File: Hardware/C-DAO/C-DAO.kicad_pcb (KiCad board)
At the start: 2 copper layers, 50 x 100 mm, 63 parts, among them J1 DIN-5, J2 Bus-connector, J3 AudioJack2, J5 Conn_02x03_Odd_Even, SW1 SW_Push_Dual, SW2 SW_Push_Dual, SW3 SW_Push_Dual, SW4 SW_Push_Dual, U1 ATmega328P-A, U2 L7805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

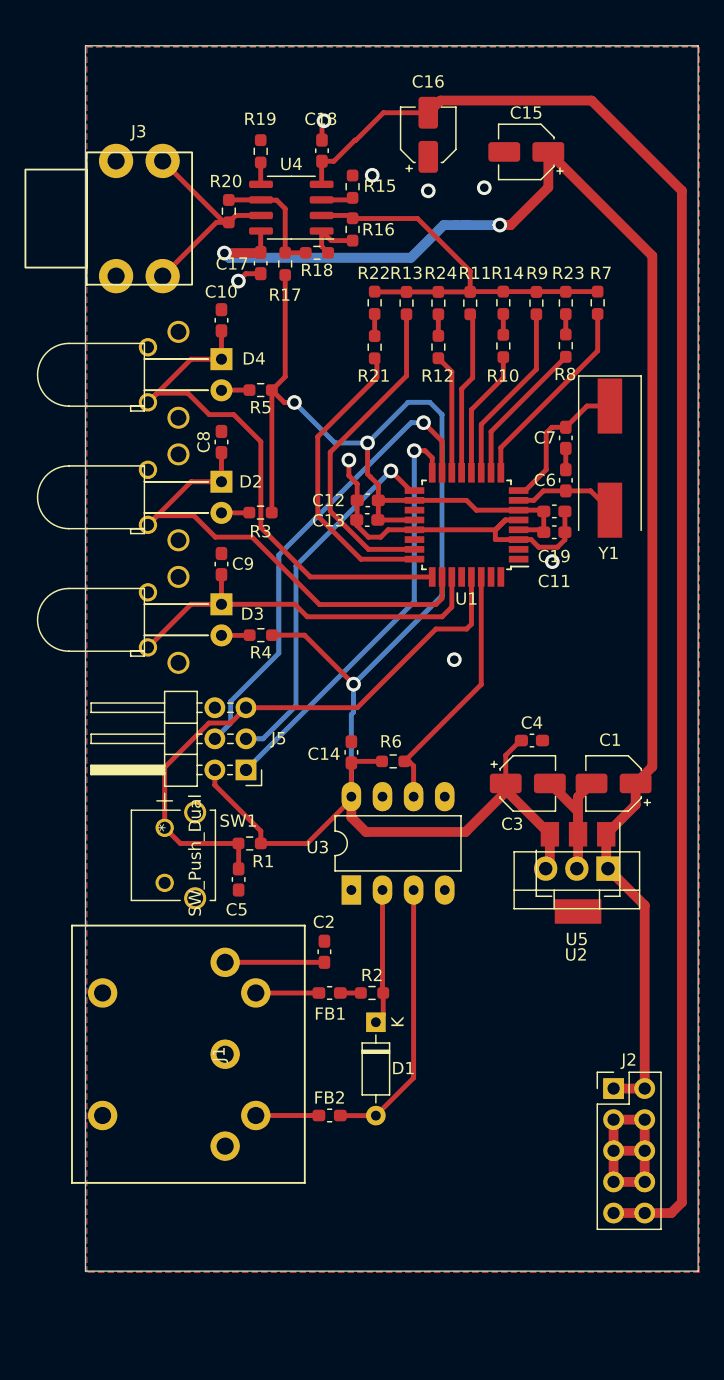
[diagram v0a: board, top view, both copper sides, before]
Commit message: Add production files and latest pcb files with bom
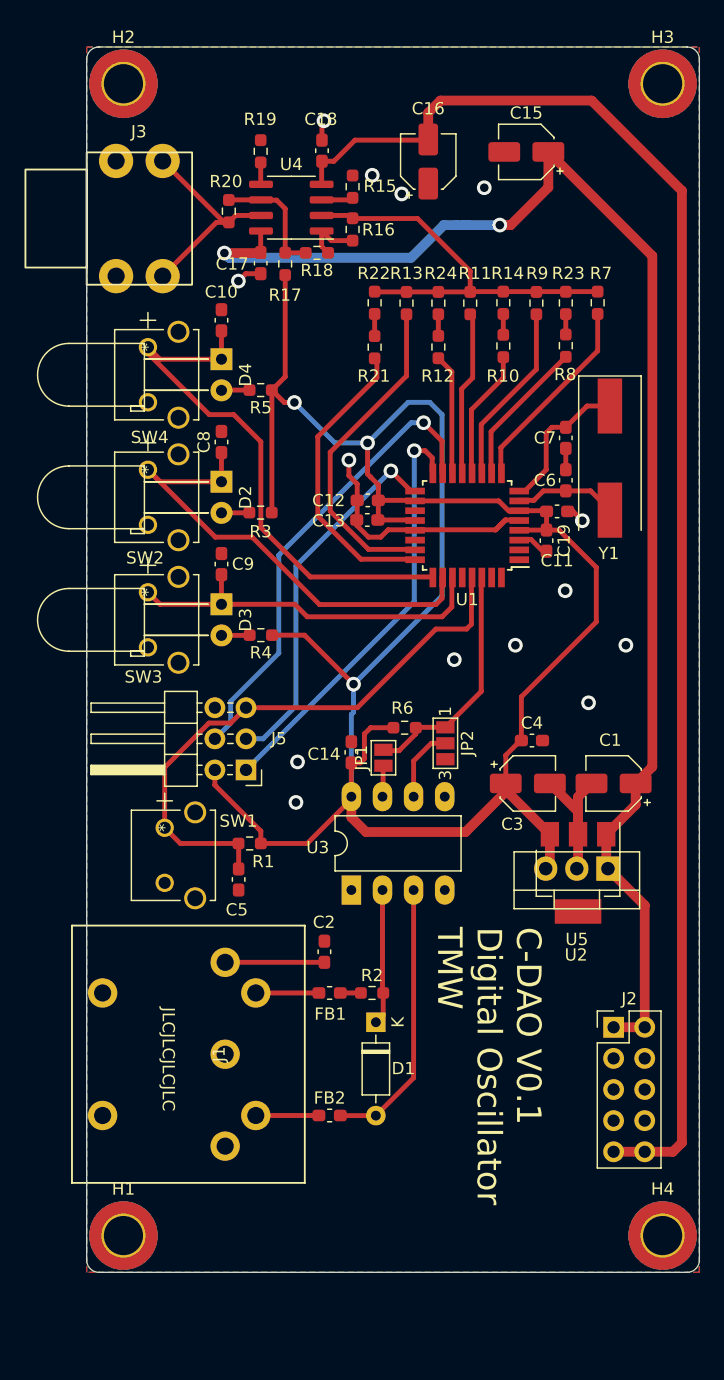
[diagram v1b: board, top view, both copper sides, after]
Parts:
- added H1: MountingHole_Pad, MountingHole:MountingHole_3.2mm_M3_DIN965_Pad_TopBottom, F.Cu at (110.0, 148.0)
- added H2: MountingHole_Pad, MountingHole:MountingHole_3.2mm_M3_DIN965_Pad_TopBottom, F.Cu at (110.0, 54.0)
- added H3: MountingHole_Pad, MountingHole:MountingHole_3.2mm_M3_DIN965_Pad_TopBottom, F.Cu at (154.0, 54.0)
- added H4: MountingHole_Pad, MountingHole:MountingHole_3.2mm_M3_DIN965_Pad_TopBottom, F.Cu at (154.0, 148.0)
- added JP1: SolderJumper_2_Open, Jumper:SolderJumper-2_P1.3mm_Open_Pad1.0x1.5mm, F.Cu at (131.2, 109.0)
- added JP2: SolderJumper_3_Open, Jumper:SolderJumper-3_P1.3mm_Open_Pad1.0x1.5mm_NumberLabels, F.Cu at (136.3, 107.8)
- D2, D3, D4: footprint LED_THT:LED_D5.0mm_Horizontal_O6.35mm_Z9.0mm -> LED_THT:LED_D5.0mm_Horizontal_O6.35mm_Z15.0mm
- J1: footprint CustomConnectors:5-pin DIN socket vertical -> footprints:5-pin DIN socket vertical
- R17, R18, R20, R3, R4, R5: value 1k -> 1.07k
- SW2, SW3, SW4: moved to F.Cu
- moved J2 5.00 mm to (150.0, 131.0)
- moved SW2 4.50 mm to (112.0, 85.5), turned to -90 degrees
- moved SW3 4.50 mm to (112.0, 95.5), turned to -90 degrees
- moved SW4 4.50 mm to (112.0, 75.5), turned to -90 degrees
- moved R6 2.90 mm to (132.9, 106.6)
- moved C19 2.47 mm to (144.5, 91.3), turned to -90 degrees
- moved C16 2.18 mm to (134.9, 60.3)
- moved C11 1.71 mm to (145.4, 88.9)
- moved U1 0.07 mm to (138.0, 90.0)
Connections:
- net Net-(D1-Pad1) renamed /MIDI_IN+
- net Net-(D1-Pad2) renamed /MIDI_IN-
- U3 pad 6: MIDI_RX -> Net-(JP2-Pad2)
- U3 pad 7: unconnected-(U3-Pad7) -> Net-(JP1-Pad1)
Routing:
- net +5V: track 158.7 -> 183.4 mm
- net GND: track 66.0 -> 43.2 mm, vias 8 -> 14
- net Net-(JP2-Pad2): track 0.00 -> 6.10 mm
- net +12V: track 122.0 -> 117.0 mm
- net -12V: track 124.9 -> 121.2 mm
- net Net-(JP1-Pad1): track 0.00 -> 2.47 mm
- net MIDI_RX: track 21.1 -> 19.7 mm
- net SEL_SQUARE: track 31.9 -> 30.8 mm
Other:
- outline, holes or cut-outs redrawn
- board text added: "C-DAO V0.1 Digital Oscillator TMW"
- board text added: "JLCJLCJLCJLC"

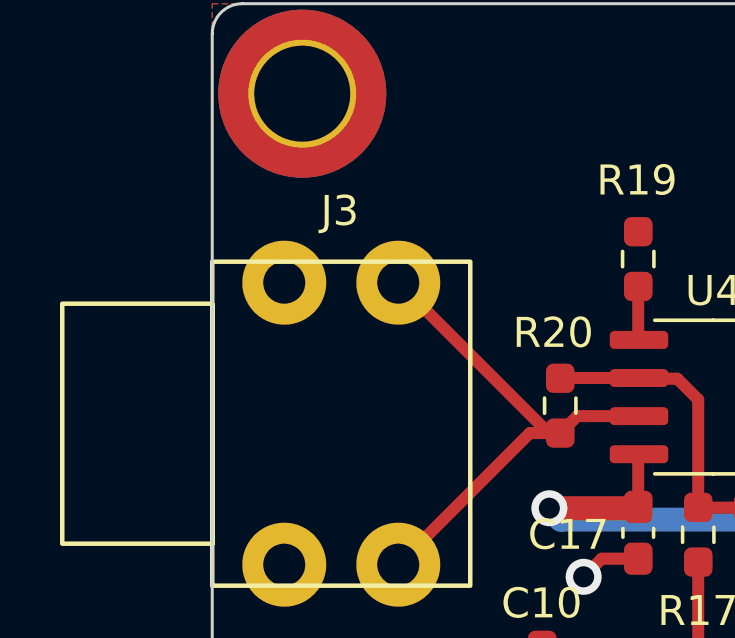
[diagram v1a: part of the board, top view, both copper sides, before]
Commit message: Update 3d models and create wrl-model from board
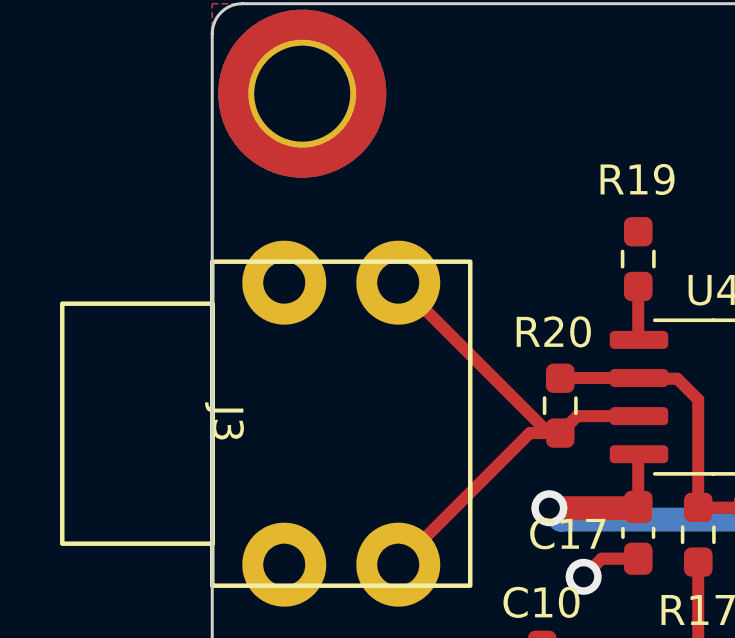
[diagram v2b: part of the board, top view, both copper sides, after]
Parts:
- J3: footprint CustomConnectors:Cliff CL13843G 3.5mm mono jack -> footprints:Cliff CL13843G 3.5mm mono jack
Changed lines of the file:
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@@
     (fp_line (start 6.6929 6.1468) (end 6.9469 6.1468) (layer "Cmts.User") (width 0.1))
     (fp_line (start -1.3081 -5.2832) (end 5.8039 -5.2832) (layer "Cmts.User") (width 0.1))
+    (fp_line (start 5.8039 -2.4892) (end 5.8039 -5.6642) (layer "Cmts.User") (width 0.1))
     (fp_line (start 5.4991 10.0838) (end 5.4991 10.3378) (layer "Cmts.User") (width 0.1))
     (fp_line (start 5.7531 10.2108) (end 5.4991 10.3378) (layer "Cmts.User") (width 0.1))
     (fp_line (start 5.8039 -5.2832) (end 5.5499 -5.4102) (layer "Cmts.User") (width 0.1))
-    (fp_line (start 5.8039 -2.4892) (end 5.8039 -5.6642) (layer "Cmts.User") (width 0.1))
     (fp_line (start 6.8199 -4.0132) (end 6.8199 2.5908) (layer "Cmts.User") (width 0.1))
     (fp_line (start 3.6449 7.6708) (end 3.8989 7.7978) (layer "Cmts.User") (width 0.1))
-    (fp_line (start 2.2479 -4.0132) (end 7.2009 -4.0132) (layer "Cmts.User") (width 0.1))
     (fp_line (start 6.8199 2.5908) (end 6.8199 6.4008) (layer "Cmts.User") (width 0.1))
     (fp_line (start 6.8199 -4.0132) (end 6.9469 -3.7592) (layer "Cmts.User") (width 0.1))
@@
     (fp_line (start 6.8199 -4.0132) (end 6.6929 -3.7592) (layer "Cmts.User") (width 0.1))
     (fp_line (start 0.8509 7.6708) (end 0.5969 7.5438) (layer "Cmts.User") (width 0.1))
+    (fp_line (start 2.2479 -4.0132) (end 7.2009 -4.0132) (layer "Cmts.User") (width 0.1))
     (fp_line (start 6.8199 6.4008) (end 6.6929 6.1468) (layer "Cmts.User") (width 0.1))
     (fp_line (start 6.6929 2.3368) (end 6.9469 2.3368) (layer "Cmts.User") (width 0.1))
@@
     )
   )
-  (footprint "CustomConnectors:Cliff CL13843G 3.5mm mono jack" (layer "F.Cu")
+  (footprint "footprints:Cliff CL13843G 3.5mm mono jack" (layer "F.Cu")
     (at 107 65 -90)
     (descr "https://www.farnell.com/datasheets/2303779.pdf")
@@
     (property "Sheetname" "")
     (attr through_hole)
-    (fp_text reference "J3" (at -7.088 -4.252 unlocked) (layer "F.SilkS")
+    (fp_text reference "J3" (at 0 -0.5 -90 unlocked) (layer "F.SilkS")
       (effects (font (size 1 1) (thickness 0.15)))
     )
@@
     (fp_rect (start 5.4 0) (end -5.4 -8.6) (layer "F.SilkS") (width 0.15) (fill none))
     (fp_rect (start 4 0) (end -4 5) (layer "F.SilkS") (width 0.15) (fill none))
+    (pad "S" thru_hole circle (at 4.7 -2.4 270) (size 2.8 2.8) (drill 1.4) (layers *.Cu *.Mask)
+      (net 2 "GND") (pintype "passive"))
     (pad "S" thru_hole circle (at -4.7 -2.4 270) (size 2.8 2.8) (drill 1.4) (layers *.Cu *.Mask)
       (net 2 "GND") (pintype "passive"))
-    (pad "S" thru_hole circle (at 4.7 -2.4 270) (size 2.8 2.8) (drill 1.4) (layers *.Cu *.Mask)
-      (net 2 "GND") (pintype "passive"))
+    (pad "T" thru_hole circle (at -4.7 -6.2 270) (size 2.8 2.8) (drill 1.4) (layers *.Cu *.Mask)
+      (net 21 "Net-(J3-PadT)") (pintype "passive"))
     (pad "T" thru_hole circle (at 4.7 -6.2 270) (size 2.8 2.8) (drill 1.4) (layers *.Cu *.Mask)
       (net 21 "Net-(J3-PadT)") (pintype "passive"))
-    (pad "T" thru_hole circle (at -4.7 -6.2 270) (size 2.8 2.8) (drill 1.4) (layers *.Cu *.Mask)
-      (net 21 "Net-(J3-PadT)") (pintype "passive"))
+    (model "C:/Users/Konrad/Documents/Kicad_Librarys/Korppulib/3dmodels/CL13843G.STEP"
+      (offset (xyz 0 0 5.5))
+      (scale (xyz 1 1 1))
+      (rotate (xyz -90 0 0))
+    )
   )
   (footprint "Connector_PinHeader_2.54mm:PinHeader_2x03_P2.54mm_Horizontal" (layer "F.Cu")
